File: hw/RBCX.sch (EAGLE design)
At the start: 472 parts, among them IC1 AMS1117-3.3, IC10 INA180A4, IC11 INA180A4, IC12 MPU-6050, IC13 STM32F103VCT6, IC2 DRV8833PWP, IC3 INA180A4, IC4 INA180A4, IC5 DRV8833PWP, IC6 INA180A4, IC7 INA180A4, IC8 INA180A4, IC9 INA180A4, P1 M1, P2 M2, P3 M3, P4 M4, Q1 NCE20P45Q, Q10 2N7002, Q2 NCE20P45Q, Q3 2N7002, Q4 2N7002, Q5 2N7002, Q6 2N7002, Q7 2N7002, Q8 2N7002, Q9 2N7002, X1 POWER_IN, X2 POWER_OUT, X3 52559-3092, X4 uUSB, Y1 5032/2P, Y2 3215_2P

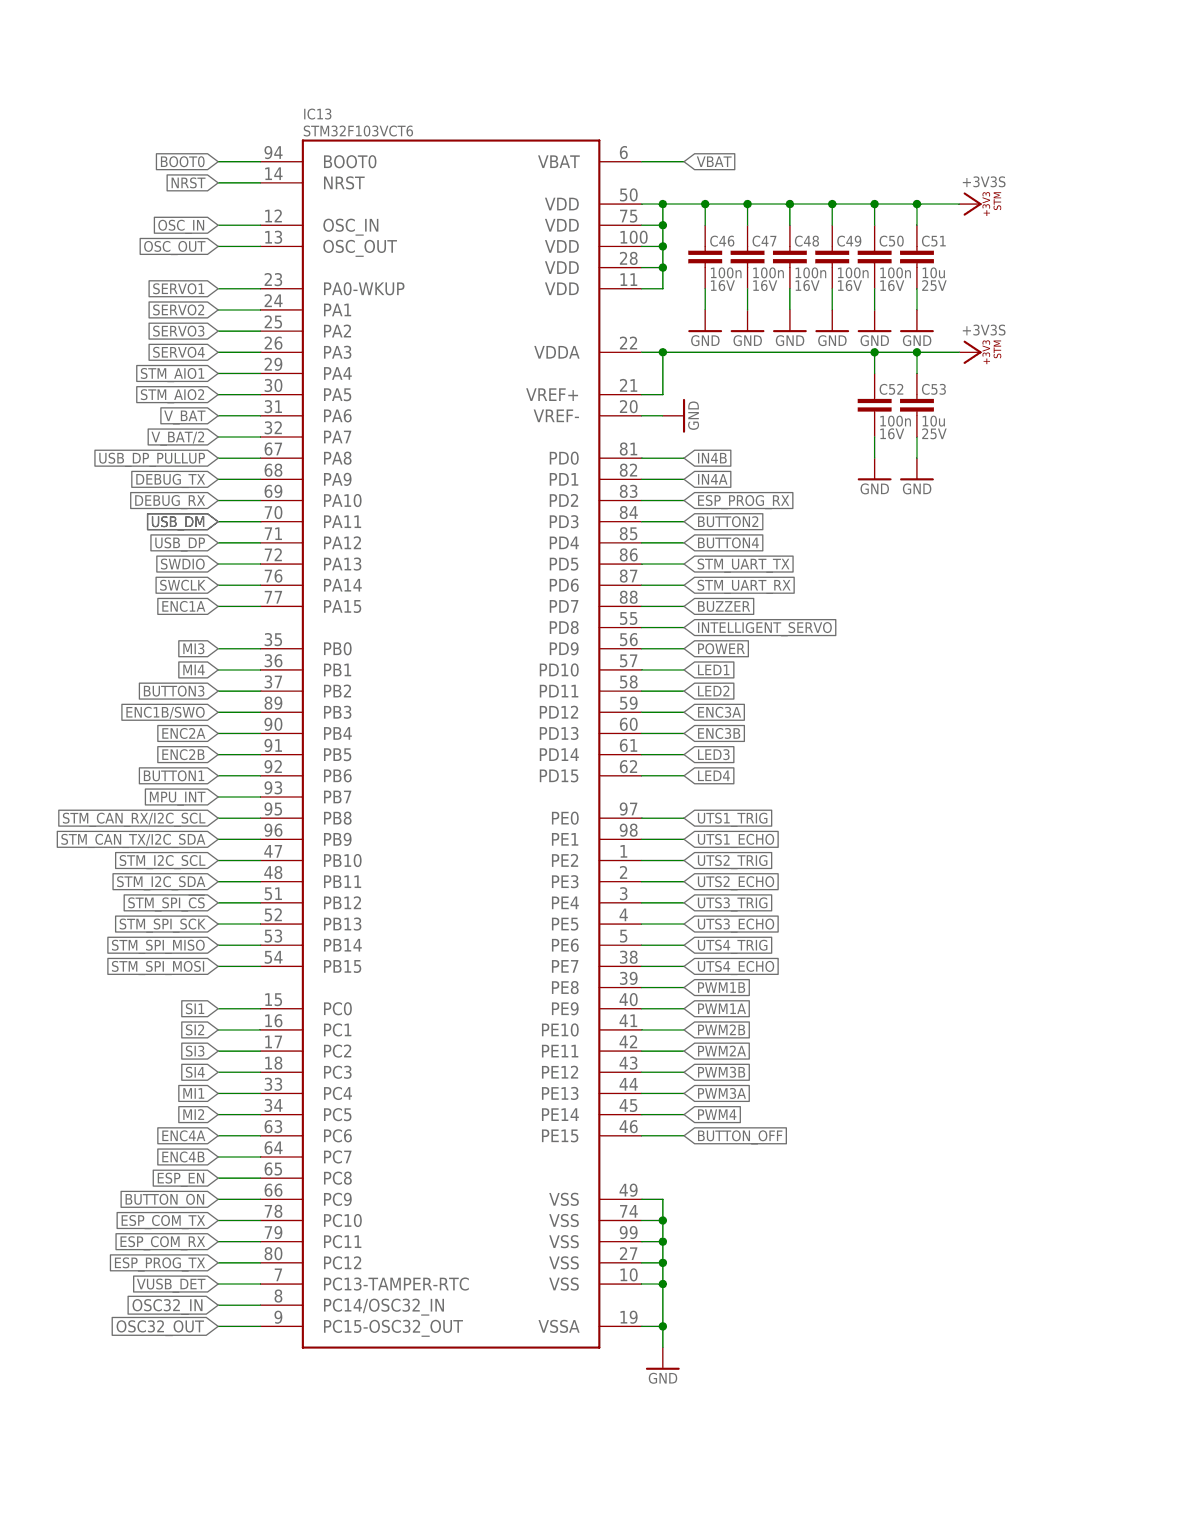
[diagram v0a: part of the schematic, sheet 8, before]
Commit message: hw: apply pinout to the schematic
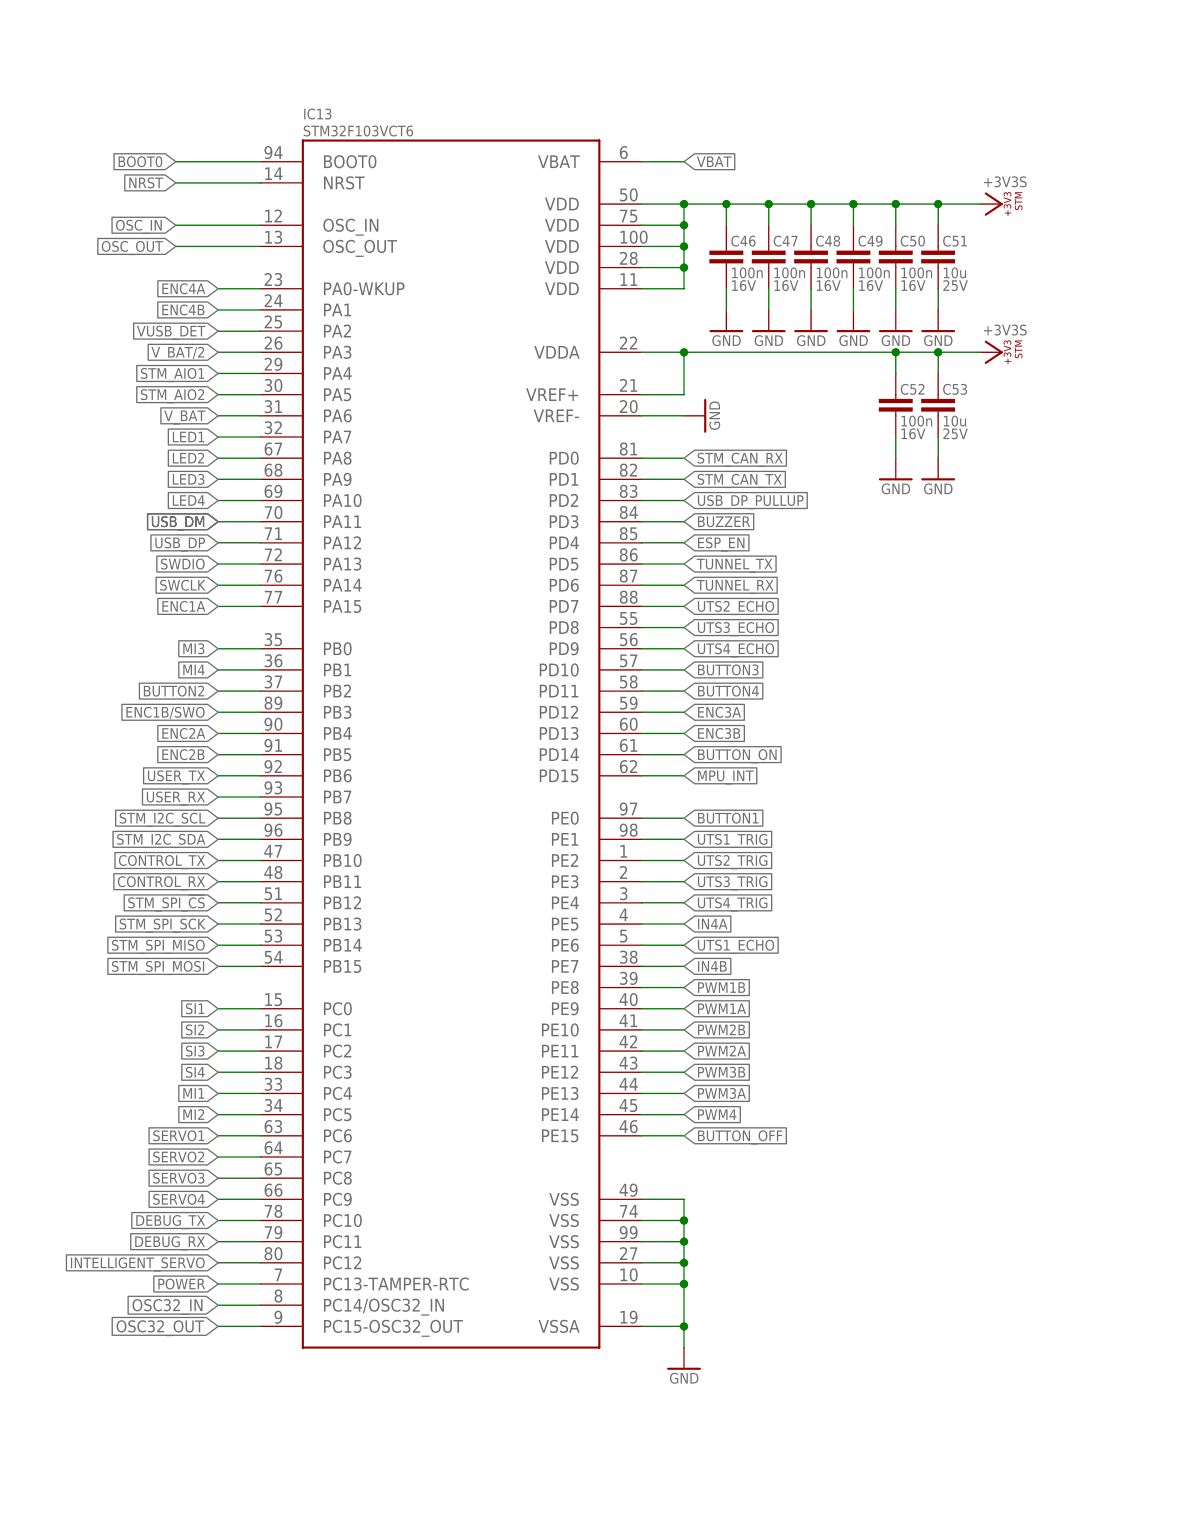
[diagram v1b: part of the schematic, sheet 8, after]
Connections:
- removed net ESP_PROG_RX: IC13.PD2, R154.2
- removed net ESP_PROG_TX: IC13.PC12, R155.2
- removed net STM_CAN_RX/I2C_SCL: IC13.PB8, R94.1
- removed net STM_CAN_TX/I2C_SDA: IC13.PB9, R93.1
- removed net STM_UART_RX: IC13.PD6, R53.1
- removed net STM_UART_TX: IC13.PD5, R52.1
- new net CONTROL_RX: IC13.PB11
- new net CONTROL_TX: IC13.PB10
- new net STM_CAN_RX: IC13.PD0, R94.1
- new net STM_CAN_TX: IC13.PD1, R93.1
- new net TUNNEL_RX: IC13.PD6, R154.2
- new net TUNNEL_TX: IC13.PD5, R155.2
- new net USER_RX: IC13.PB7, R53.1
- new net USER_TX: IC13.PB6, R52.1
- net BUTTON1: now also IC13.PE0; no longer IC13.PB6
- net BUTTON2: now also IC13.PB2; no longer IC13.PD3
- net BUTTON3: now also IC13.PD10; no longer IC13.PB2
- net BUTTON4: now also IC13.PD11; no longer IC13.PD4
- net BUTTON_ON: now also IC13.PD14; no longer IC13.PC9
- net BUZZER: now also IC13.PD3; no longer IC13.PD7
- net DEBUG_RX: now also IC13.PC11; no longer IC13.PA10
- net DEBUG_TX: now also IC13.PC10; no longer IC13.PA9
- net ENC4A: now also IC13.PA0-WKUP; no longer IC13.PC6
- net ENC4B: now also IC13.PA1; no longer IC13.PC7
- net ESP_COM_RX: no longer IC13.PC11
- net ESP_COM_TX: no longer IC13.PC10
- net ESP_EN: now also IC13.PD4; no longer IC13.PC8
- net IN4A: now also IC13.PE5; no longer IC13.PD1
- net IN4B: now also IC13.PE7; no longer IC13.PD0
- net INTELLIGENT_SERVO: now also IC13.PC12; no longer IC13.PD8
- net LED1: now also IC13.PA7; no longer IC13.PD10
- net LED2: now also IC13.PA8; no longer IC13.PD11
- net LED3: now also IC13.PA9; no longer IC13.PD14
- net LED4: now also IC13.PA10; no longer IC13.PD15
- net MPU_INT: now also IC13.PD15; no longer IC13.PB7
- net POWER: now also IC13.PC13-TAMPER-RTC; no longer IC13.PD9
- net SERVO1: now also IC13.PC6; no longer IC13.PA0-WKUP
- net SERVO2: now also IC13.PC7; no longer IC13.PA1
- net SERVO3: now also IC13.PC8; no longer IC13.PA2
- net SERVO4: now also IC13.PC9; no longer IC13.PA3
- net STM_I2C_SCL: now also IC13.PB8; no longer IC13.PB10
- net STM_I2C_SDA: now also IC13.PB9; no longer IC13.PB11
- net USB_DP_PULLUP: now also IC13.PD2; no longer IC13.PA8
- net UTS1_ECHO: now also IC13.PE6; no longer IC13.PE1
- net UTS1_TRIG: now also IC13.PE1; no longer IC13.PE0
- net UTS2_ECHO: now also IC13.PD7; no longer IC13.PE3
- net UTS3_ECHO: now also IC13.PD8; no longer IC13.PE5
- net UTS3_TRIG: now also IC13.PE3; no longer IC13.PE4
- net UTS4_ECHO: now also IC13.PD9; no longer IC13.PE7
- net UTS4_TRIG: now also IC13.PE4; no longer IC13.PE6
- net VUSB_DET: now also IC13.PA2; no longer IC13.PC13-TAMPER-RTC
- net V_BAT/2: now also IC13.PA3; no longer IC13.PA7
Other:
- moved on the sheet: C46, C47, C48, C49, C50, C51, C52, C53

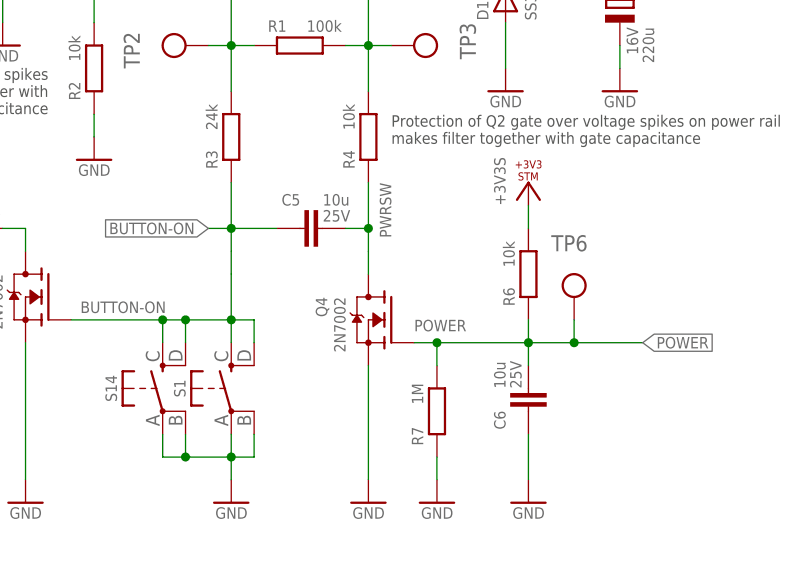
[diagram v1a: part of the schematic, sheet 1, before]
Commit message: hw: fix power circuit capacitors value
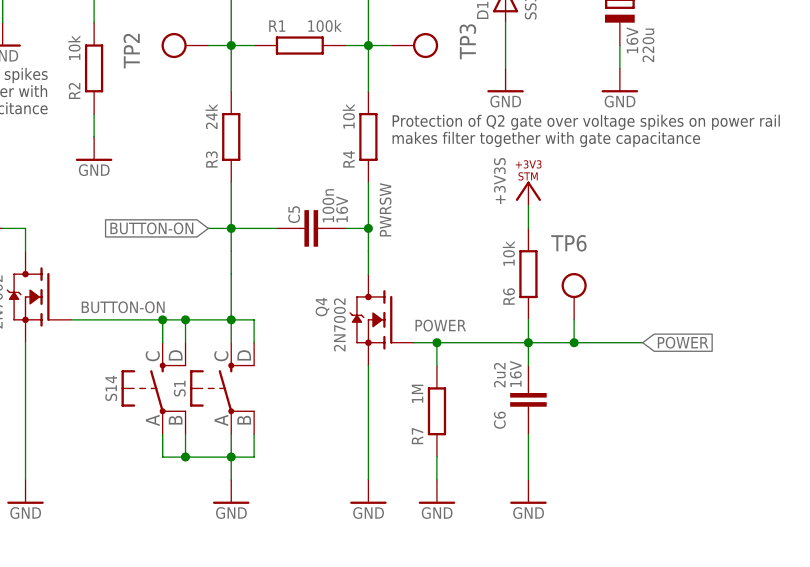
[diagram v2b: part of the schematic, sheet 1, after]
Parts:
- C5: value 10u -> 100n; device rcl_upravena:C-EUC0805 -> rcl_upravena:C-EUC0402; VOLTAGE 25V -> 16V
- C6: value 10u -> 2u2; device rcl_upravena:C-EUC0805 -> rcl_upravena:C-EUC0603; VOLTAGE 25V -> 16V

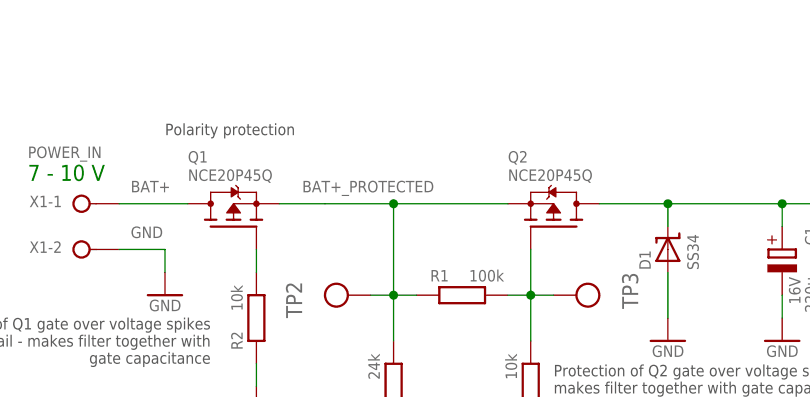
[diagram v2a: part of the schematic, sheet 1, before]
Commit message: hw: fix power button function without battery connected (only in schematic)
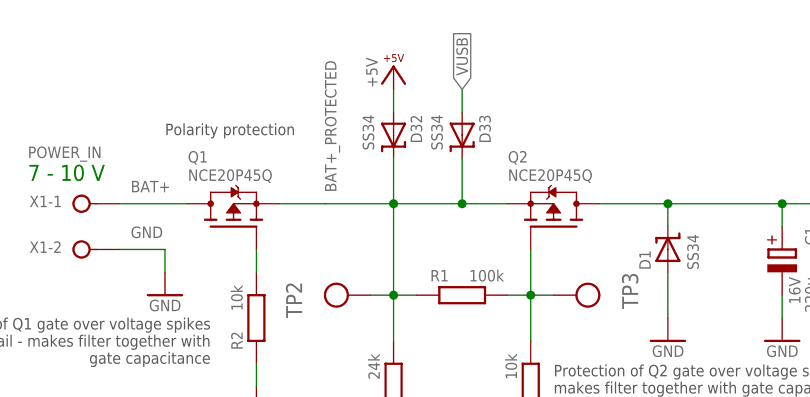
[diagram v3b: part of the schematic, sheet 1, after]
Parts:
- added D32, D33: SS34, diode:SHOTTKY-SMA
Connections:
- net +5V: now also D32.A
- net BAT+_PROTECTED: now also D32.C, D33.C
- net VUSB: now also D33.A
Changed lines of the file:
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@@
 <attribute name="VOLTAGE" value="16V"/>
 </part>
+<part name="D32" library="diode" deviceset="SHOTTKY" device="-SMA" value="SS34"/>
+<part name="P+45" library="Supply" deviceset="+5V" device=""/>
+<part name="D33" library="diode" deviceset="SHOTTKY" device="-SMA" value="SS34"/>
 </parts>
 <sheets>
@@
 <attribute name="VOLTAGE" x="121.158" y="160.02" size="1.27" layer="96" rot="R90"/>
 </instance>
+<instance part="D32" gate="G$1" x="88.9" y="215.9" smashed="yes" rot="R270">
+<attribute name="NAME" x="90.805" y="218.186" size="1.27" layer="95" rot="R270"/>
+<attribute name="VALUE" x="86.741" y="218.186" size="1.27" layer="96" rot="MR270"/>
+</instance>
+<instance part="P+45" gate="1" x="88.9" y="223.52" smashed="yes">
+<attribute name="VALUE" x="87.122" y="224.536" size="1.27" layer="96" rot="MR270"/>
+</instance>
+<instance part="D33" gate="G$1" x="96.52" y="215.9" smashed="yes" rot="R270">
+<attribute name="NAME" x="98.425" y="218.186" size="1.27" layer="95" rot="R270"/>
+<attribute name="VALUE" x="94.361" y="218.186" size="1.27" layer="96" rot="MR270"/>
+</instance>
 </instances>
 <busses>
@@
 <wire x1="76.2" y1="208.28" x2="81.28" y2="208.28" width="0.1524" layer="91"/>
 <wire x1="81.28" y1="208.28" x2="88.9" y2="208.28" width="0.1524" layer="91"/>
-<wire x1="88.9" y1="208.28" x2="101.6" y2="208.28" width="0.1524" layer="91"/>
-<label x="78.74" y="209.55" size="1.27" layer="95"/>
+<wire x1="88.9" y1="208.28" x2="96.52" y2="208.28" width="0.1524" layer="91"/>
+<label x="82.55" y="209.55" size="1.27" layer="95" rot="R90"/>
 <pinref part="Q1" gate="G$1" pin="S"/>
 <pinref part="R1" gate="G$1" pin="1"/>
+<wire x1="96.52" y1="208.28" x2="101.6" y2="208.28" width="0.1524" layer="91"/>
 <wire x1="91.44" y1="198.12" x2="88.9" y2="198.12" width="0.1524" layer="91"/>
 <wire x1="88.9" y1="198.12" x2="88.9" y2="208.28" width="0.1524" layer="91"/>
@@
 <pinref part="TP2" gate="G$1" pin="TP"/>
 <wire x1="86.36" y1="198.12" x2="88.9" y2="198.12" width="0.1524" layer="91"/>
+<pinref part="D32" gate="G$1" pin="C"/>
+<wire x1="88.9" y1="213.36" x2="88.9" y2="208.28" width="0.1524" layer="91"/>
+<pinref part="D33" gate="G$1" pin="C"/>
+<wire x1="96.52" y1="213.36" x2="96.52" y2="208.28" width="0.1524" layer="91"/>
+<junction x="96.52" y="208.28"/>
 </segment>
 </net>
@@
 <junction x="317.5" y="96.52"/>
 <pinref part="P+39" gate="1" pin="+5V"/>
+</segment>
+<segment>
+<pinref part="P+45" gate="1" pin="+5V"/>
+<pinref part="D32" gate="G$1" pin="A"/>
+<wire x1="88.9" y1="220.98" x2="88.9" y2="218.44" width="0.1524" layer="91"/>
 </segment>
 </net>
@@
 <wire x1="261.62" y1="187.96" x2="264.16" y2="187.96" width="0.1524" layer="91"/>
 </segment>
+<segment>
+<pinref part="D33" gate="G$1" pin="A"/>
+<wire x1="96.52" y1="218.44" x2="96.52" y2="220.98" width="0.1524" layer="91"/>
+<label x="96.52" y="220.98" size="1.27" layer="95" rot="R90" xref="yes"/>
+</segment>
 </net>

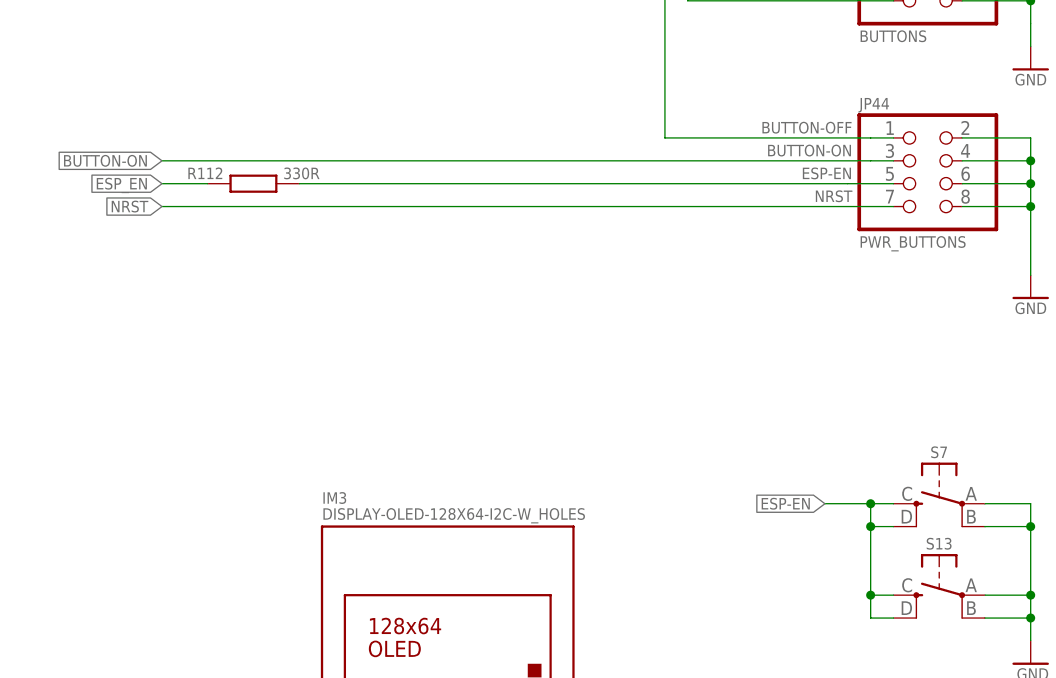
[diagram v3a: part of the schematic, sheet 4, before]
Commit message: hw: remove resistor between STM and ESP enable
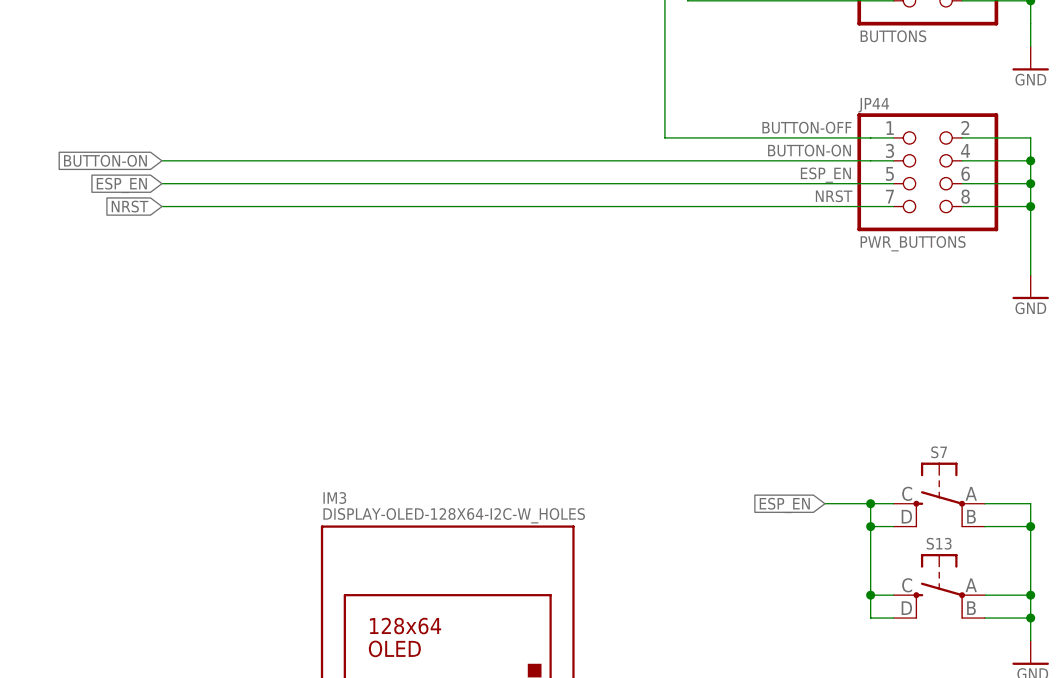
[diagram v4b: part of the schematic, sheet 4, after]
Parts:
- removed R112: 330R, rcl_upravena:R-EU_R0402
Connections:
- removed net ESP-EN: IM9.EN, JP44.5, R112.2, S13.S, S13.S1, S7.S, S7.S1, TP60.TP, X3-15.S
- net ESP_EN: now also IM9.EN, JP44.5, S13.S, S13.S1, S7.S, S7.S1, TP60.TP, X3-15.S; no longer R112.1
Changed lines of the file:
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@@
 <part name="JP44" library="pinhead" library_urn="urn:adsk.eagle:library:325" deviceset="PINHD-2X4" device="" package3d_urn="urn:adsk.eagle:package:22461/2" value="PWR_BUTTONS"/>
 <part name="GND111" library="Supply" deviceset="GND" device=""/>
-<part name="R112" library="rcl_upravena" deviceset="R-EU_" device="R0402" value="330R"/>
 <part name="GND113" library="Supply" deviceset="GND" device=""/>
 <part name="+3V29" library="Supply" deviceset="+3V3S" device=""/>
@@
 </segment>
 </net>
-<net name="ESP-EN" class="0">
+<net name="ESP_EN" class="0">
 <segment>
 <wire x1="317.5" y1="195.58" x2="309.88" y2="195.58" width="0.1524" layer="91"/>
@@
 <attribute name="VALUE" x="165.862" y="99.822" size="1.27" layer="96"/>
 </instance>
-<instance part="R112" gate="G$1" x="81.28" y="114.3" smashed="yes">
-<attribute name="NAME" x="77.978" y="114.808" size="1.27" layer="95" rot="MR0"/>
-<attribute name="VALUE" x="84.582" y="114.808" size="1.27" layer="96"/>
-</instance>
 <instance part="IM4" gate="G$1" x="147.32" y="25.4" smashed="yes">
 <attribute name="NAME" x="121.92" y="35.56" size="1.27" layer="95"/>
@@
 </segment>
 </net>
-<net name="ESP-EN" class="0">
+<net name="ESP_EN" class="0">
 <segment>
-<pinref part="R112" gate="G$1" pin="2"/>
-<wire x1="86.36" y1="114.3" x2="147.32" y2="114.3" width="0.1524" layer="91"/>
+<label x="71.12" y="114.3" size="1.27" layer="95" rot="MR0" xref="yes"/>
+<wire x1="71.12" y1="114.3" x2="152.4" y2="114.3" width="0.1524" layer="91"/>
 <pinref part="JP44" gate="A" pin="5"/>
-<wire x1="147.32" y1="114.3" x2="152.4" y2="114.3" width="0.1524" layer="91"/>
 <label x="147.828" y="114.808" size="1.27" layer="95" rot="MR0"/>
 </segment>
@@
 </segment>
 </net>
-<net name="ESP_EN" class="0">
-<segment>
-<pinref part="R112" gate="G$1" pin="1"/>
-<wire x1="76.2" y1="114.3" x2="71.12" y2="114.3" width="0.1524" layer="91"/>
-<label x="71.12" y="114.3" size="1.27" layer="95" rot="MR0" xref="yes"/>
-</segment>
-</net>
 <net name="BUZZER" class="0">
 <segment>
@@
 </segment>
 </net>
-<net name="ESP-EN" class="0">
+<net name="ESP_EN" class="0">
 <segment>
 <pinref part="IM9" gate="G$1" pin="EN"/>
